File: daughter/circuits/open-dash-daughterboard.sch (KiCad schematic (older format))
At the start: 10 parts, among them J1 Conn_01x01_Female, J2 Conn_01x01_Female, J3 Conn_01x01_Female, J4 Conn_01x01_Female, J43 Conn_02x02_Counter_Clockwise, J5 Conn_02x06_Odd_Even, J6 Conn_IDE_40, J7 Conn_IDE_40, J8 Conn_IDE_40

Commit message: Added model for c6 corvette housing. Also added code for soft shutdown. Still need to detect main comp current.
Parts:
- D1: symbol Open_Automation:D_1N5819HW -> open-dash-daughterboard-rescue:D_1N5819HW-Open_Automation
- J6, J7, J8: symbol Open_Automation:Conn_IDE_40 -> open-dash-daughterboard-rescue:Conn_IDE_40-Open_Automation
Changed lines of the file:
@@
 	6600 2550 6550 2550
 $Comp
-L Open_Automation:Conn_IDE_40 J6
+L open-dash-daughterboard-rescue:Conn_IDE_40-Open_Automation J6
 U 1 1 659B5A32
 P 6250 2350
@@
 $EndComp
 $Comp
-L Open_Automation:Conn_IDE_40 J8
+L open-dash-daughterboard-rescue:Conn_IDE_40-Open_Automation J8
 U 1 1 659BC0F8
 P 11300 2350
@@
 	9050 2950 9000 2950
 $Comp
-L Open_Automation:Conn_IDE_40 J7
+L open-dash-daughterboard-rescue:Conn_IDE_40-Open_Automation J7
 U 1 1 659BAB3D
 P 8700 2350
@@
 RF-
 $Comp
-L Open_Automation:D_1N5819HW D1
+L open-dash-daughterboard-rescue:D_1N5819HW-Open_Automation D1
 U 1 1 6076B14B
 P 1700 2500

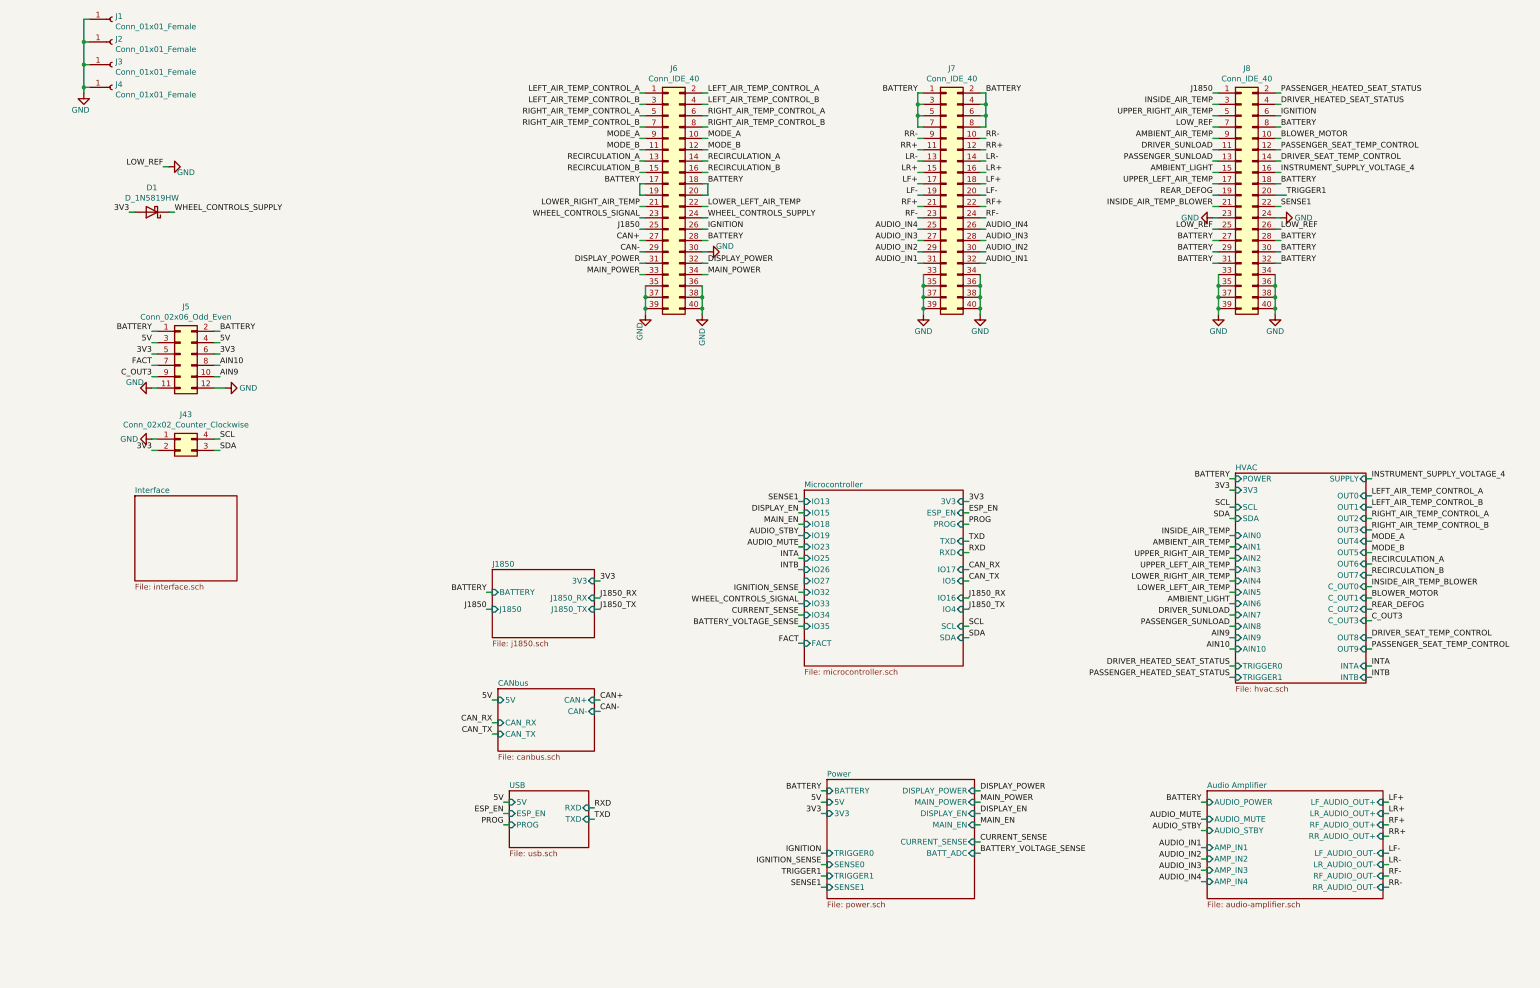
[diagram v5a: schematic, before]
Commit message: Added external amp trigger code and circuit to PCB. Made some layout modifications.
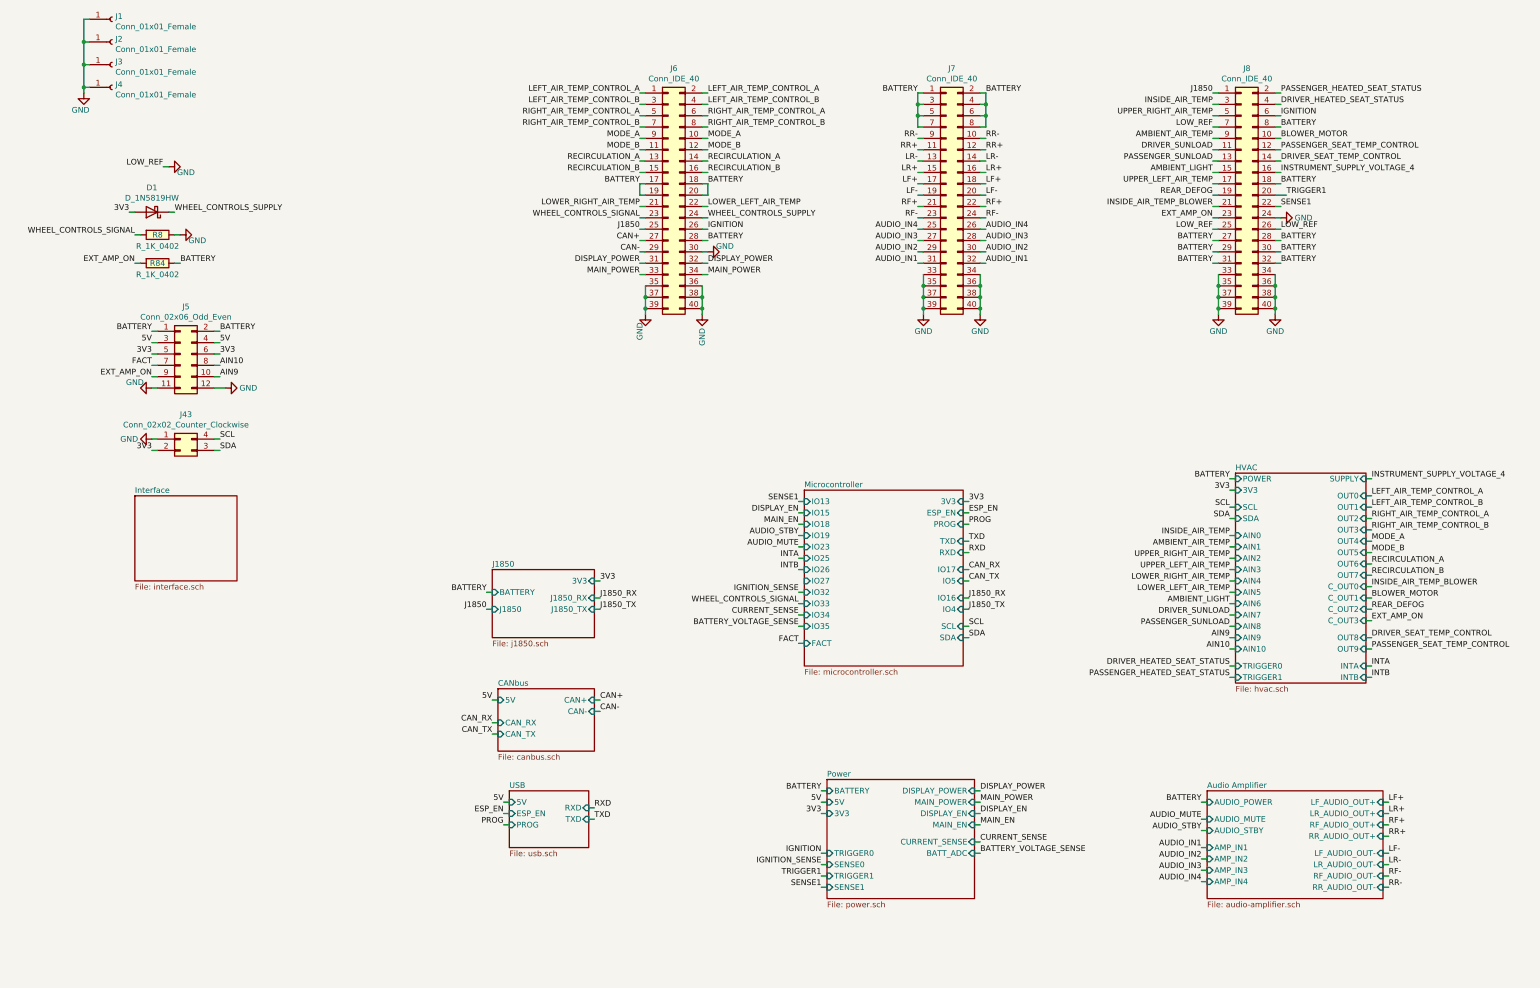
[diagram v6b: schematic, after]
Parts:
- added R8, R84: R_1K_0402, Resistor_SMD:R_0402_1005Metric_Pad0.72x0.64mm_HandSolder, symbol Open_Automation:R_1K_0402
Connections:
- net BATTERY: now also R84.1
- net GND: now also R8.1; no longer J8.23 (Pin_23)
- net WHEEL_CONTROLS_SIGNAL: now also R8.2
- net C_OUT3 renamed EXT_AMP_ON
- net EXT_AMP_ON: now also J8.23 (Pin_23), R84.2
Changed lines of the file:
@@
 BATTERY
 Text Label 12450 6100 0    50   ~ 0
-C_OUT3
+EXT_AMP_ON
 Text Label 11200 5350 2    50   ~ 0
 INSIDE_AIR_TEMP
@@
 Wire Wire Line
 	11650 1450 11600 1450
-$Comp
-L open-dash-daughterboard-rescue:GND-power #PWR?
-U 1 1 6387A525
-P 11050 2550
-AR Path="/5ABD187E/6387A525" Ref="#PWR?"  Part="1"
-AR Path="/6387A525" Ref="#PWR015"  Part="1"
-AR Path="/5A7BADB8/6387A525" Ref="#PWR?"  Part="1"
-AR Path="/62CC146C/6387A525" Ref="#PWR?"  Part="1"
-F 0 "#PWR015" H 11050 2300 50  0001 C CNN
-F 1 "GND" V 11050 2350 50  0000 C CNN
-F 2 "" H 11050 2550 50  0001 C CNN
-F 3 "" H 11050 2550 50  0001 C CNN
-	1    11050 2550
-	0    1    1    0
-$EndComp
 Wire Wire Line
 	11050 2550 11100 2550
@@
 3V3
 Text Label 1700 3950 2    50   ~ 0
-C_OUT3
+EXT_AMP_ON
 Wire Wire Line
 	1700 3950 1750 3950
@@
 	-1   0    0    1
 $EndComp
+Text Label 1550 2700 2    50   ~ 0
+WHEEL_CONTROLS_SIGNAL
+$Comp
+L Open_Automation:R_1K_0402 R8
+U 1 1 618E7527
+P 1750 2700
+F 0 "R8" V 1750 2700 50  0000 C CNN
+F 1 "R_1K_0402" V 1850 2700 50  0000 C CNN
+F 2 "Resistor_SMD:R_0402_1005Metric_Pad0.72x0.64mm_HandSolder" V 1680 2700 50  0001 C CNN
+F 3 "https://www.digikey.com/product-detail/en/panasonic-electronic-components/ERJ-3GEYJ102V/P1.0KGDKR-ND/577615" V 1830 2700 50  0001 C CNN
+F 4 "0402WGF1001TCE" V 1930 2800 60  0001 C CNN "Part Number"
+F 5 "C11702" H 1750 2700 50  0001 C CNN "LCSC"
+	1    1750 2700
+	0    1    1    0
+$EndComp
+Wire Wire Line
+	1550 2700 1600 2700
+$Comp
+L open-dash-daughterboard-rescue:GND-power #PWR?
+U 1 1 619049B0
+P 1950 2700
+AR Path="/5ABD187E/619049B0" Ref="#PWR?"  Part="1"
+AR Path="/619049B0" Ref="#PWR0149"  Part="1"
+AR Path="/5A7BADB8/619049B0" Ref="#PWR?"  Part="1"
+F 0 "#PWR0149" H 1950 2450 50  0001 C CNN
+F 1 "GND" V 1900 2550 50  0000 C CNN
+F 2 "" H 1950 2700 50  0001 C CNN
+F 3 "" H 1950 2700 50  0001 C CNN
+	1    1950 2700
+	0    -1   -1   0
+$EndComp
+Wire Wire Line
+	1950 2700 1900 2700
+$Comp
+L Open_Automation:R_1K_0402 R84
+U 1 1 61961BCF
+P 1750 2950
+F 0 "R84" V 1750 2950 50  0000 C CNN
+F 1 "R_1K_0402" V 1850 2950 50  0000 C CNN
+F 2 "Resistor_SMD:R_0402_1005Metric_Pad0.72x0.64mm_HandSolder" V 1680 2950 50  0001 C CNN
+F 3 "https://www.digikey.com/product-detail/en/panasonic-electronic-components/ERJ-3GEYJ102V/P1.0KGDKR-ND/577615" V 1830 2950 50  0001 C CNN
+F 4 "0402WGF1001TCE" V 1930 3050 60  0001 C CNN "Part Number"
+F 5 "C11702" H 1750 2950 50  0001 C CNN "LCSC"
+	1    1750 2950
+	0    1    1    0
+$EndComp
+Wire Wire Line
+	1550 2950 1600 2950
+Wire Wire Line
+	1950 2950 1900 2950
+Text Label 1550 2950 2    50   ~ 0
+EXT_AMP_ON
+Text Label 1950 2950 0    50   ~ 0
+BATTERY
+Text Label 11050 2550 2    50   ~ 0
+EXT_AMP_ON
 $EndSCHEMATC

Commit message: Using npn-pnp high side switch for ext amp trigger.
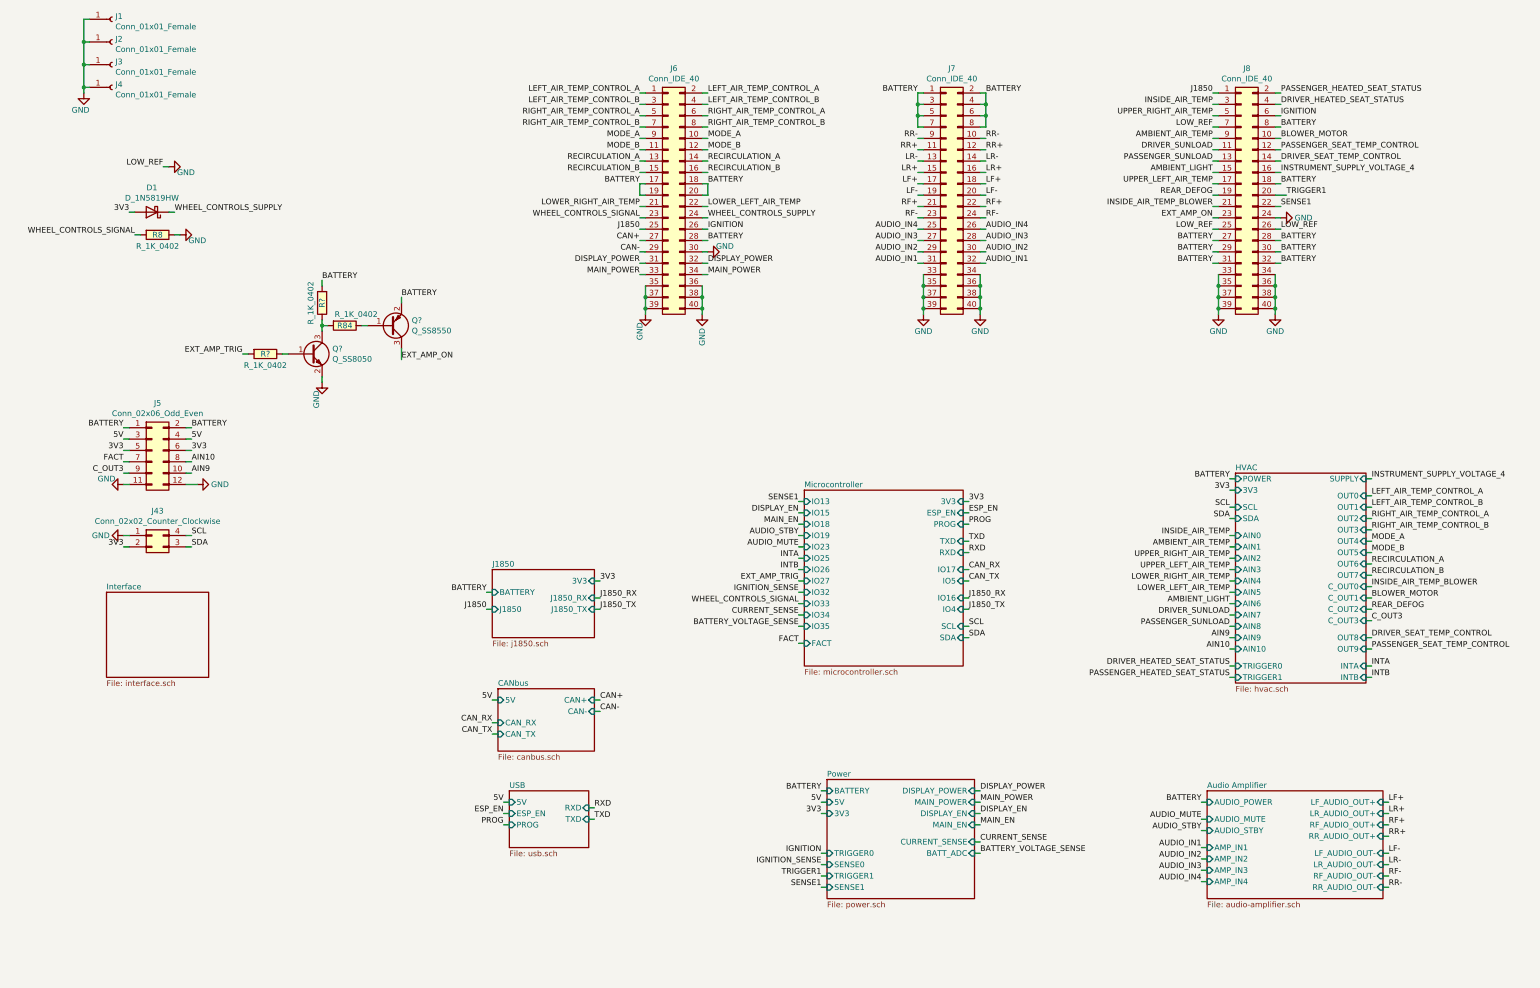
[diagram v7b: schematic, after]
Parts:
- added Q?: Q_SS8550, Package_TO_SOT_SMD:SOT-23, symbol Open_Automation:Q_SS8550
- added Q?: Q_SS8050, Package_TO_SOT_SMD:SOT-23, symbol Open_Automation:Q_SS8050
- added R? (x2): R_1K_0402, Resistor_SMD:R_0402_1005Metric_Pad0.72x0.64mm_HandSolder, symbol Open_Automation:R_1K_0402
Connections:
- net BATTERY: now also Q?.2 (E), R?.2; no longer R84.1
- net EXT_AMP_ON: now also Q?.3 (C); no longer J5.9 (Pin_9), R84.2
- net GND: now also Q?.2 (E)
- new net: Q?.1 (B), R84.1
- new net: Q?.3 (C), R84.2, R?.1
- new net: Q?.1 (B), R?.1
- new net C_OUT3: J5.9 (Pin_9)
- new net EXT_AMP_TRIG: R?.2
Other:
- moved on the sheet: J43, J5, R84
